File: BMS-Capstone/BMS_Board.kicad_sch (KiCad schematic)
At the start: 32 parts, among them IC1 MP2643, IC2 MP2643, Q1 FODM121, Q2 FODM121, Q3 FODM121, Q4 FODM121

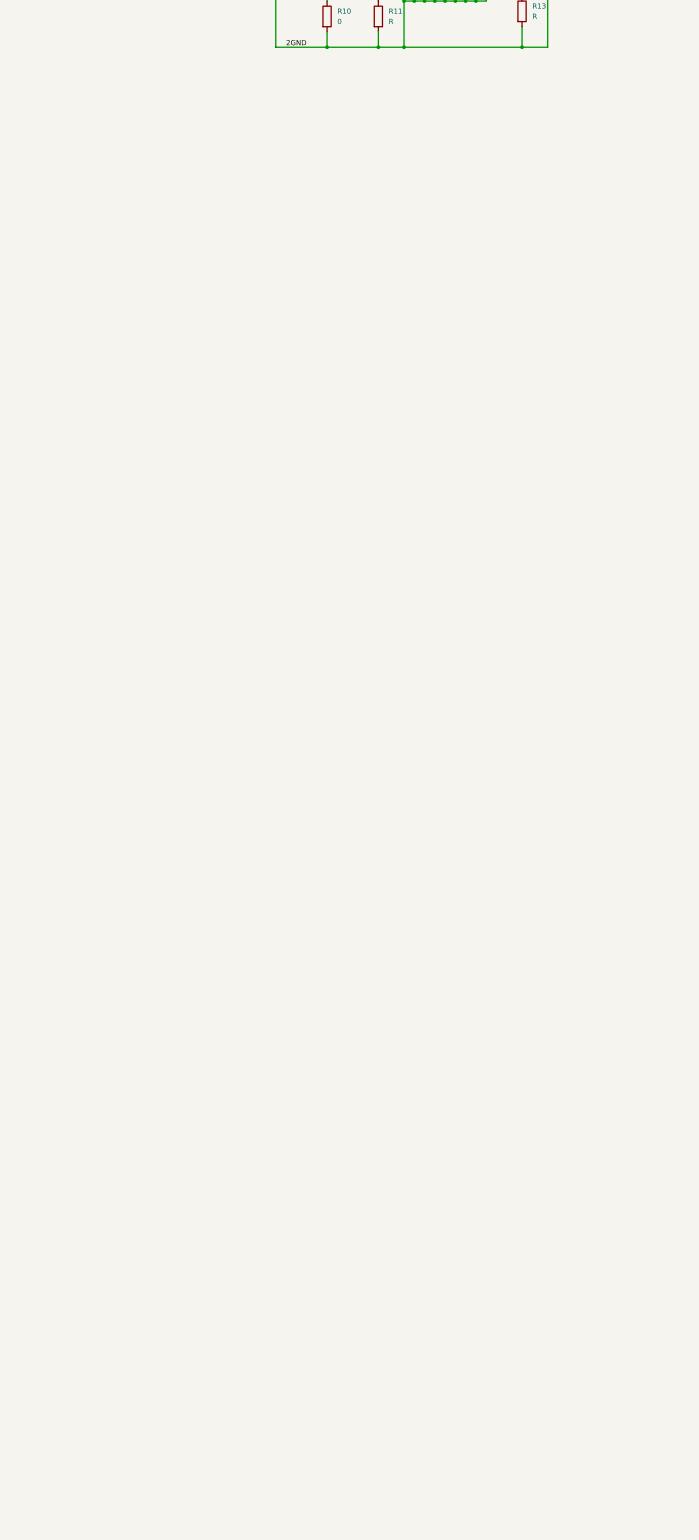
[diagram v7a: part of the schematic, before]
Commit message: Added 4 balancing boards
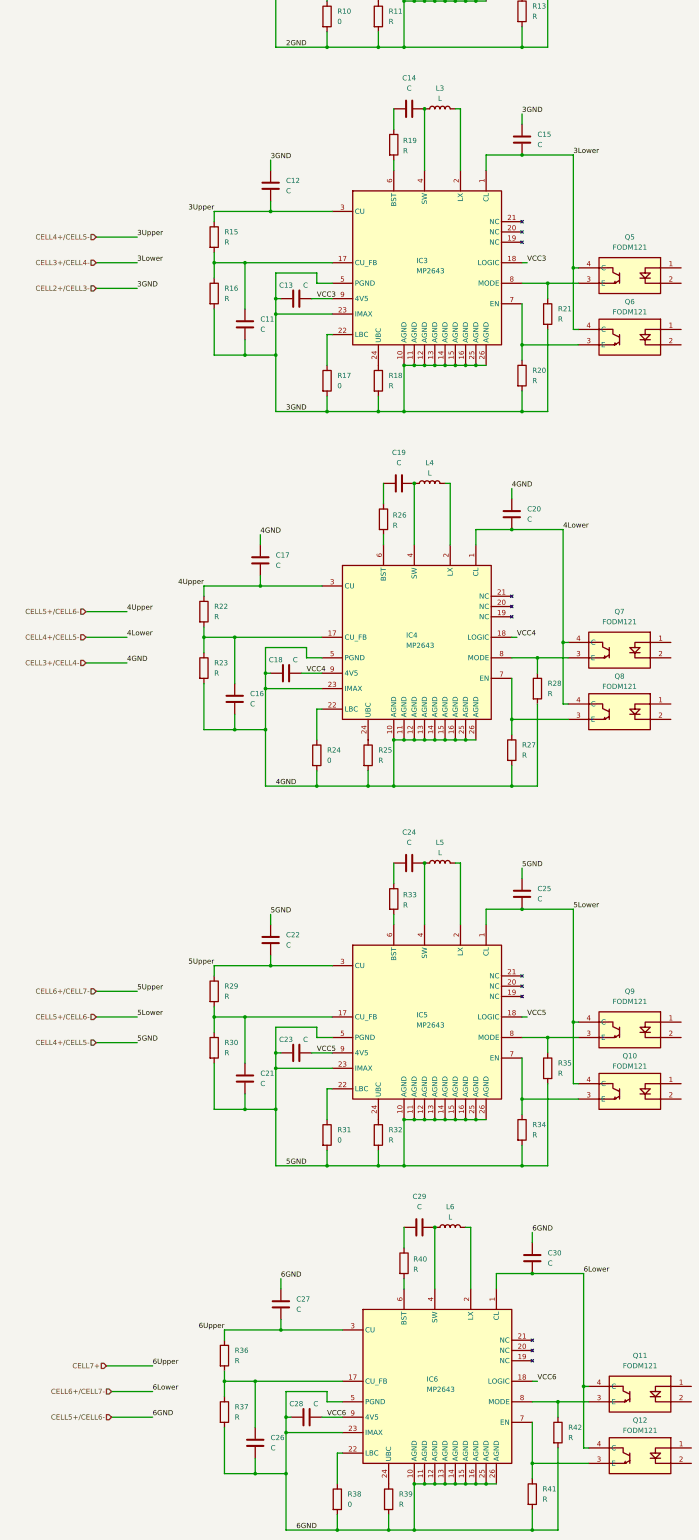
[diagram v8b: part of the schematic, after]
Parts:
- added C11, C12, C13, C14, C15, C16, C17, C18, C19, C20, C21, C22, C23, C24, C25, C26, C27, C28, C29, C30: C, Capacitor_SMD:C_0805_2012Metric, symbol Device:C
- added IC3, IC4, IC5, IC6: MP2643, SamacSys_Parts:MP2639AGRZ, symbol SamacSys_Parts:MP2643
- added L3, L4, L5, L6: L, SamacSys_Parts:MPLAL4020R47 Inductor, symbol Device:L
- added Q10, Q11, Q12, Q5, Q6, Q7, Q8, Q9: FODM121, SamacSys_Parts:SOP254P675X240-4N, symbol SamacSys_Parts:FODM121
- added R15, R16, R18, R19, R20, R21, R22, R23, R25, R26, R27, R28, R29, R30, R32, R33, R34, R35, R36, R37, R39, R40, R41, R42: R, Resistor_SMD:R_0805_2012Metric, symbol Device:R
- added R17, R24, R31, R38: 0, Resistor_SMD:R_0805_2012Metric, symbol Device:R
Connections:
- net CELL2+/CELL3-: now also C11.1, C12.2, C13.1, C15.2, IC3.10 (AGND), IC3.11 (AGND), IC3.12 (AGND), IC3.13 (AGND), IC3.14 (AGND), IC3.15 (AGND), IC3.16 (AGND), IC3.23 (IMAX), IC3.25 (AGND), IC3.26 (AGND), IC3.5 (PGND), R16.2, R17.2, R18.2, R20.2, R21.2
- net CELL3+/CELL4-: now also C15.1, C16.1, C17.2, C18.1, C20.2, IC3.1 (CL), IC4.10 (AGND), IC4.11 (AGND), IC4.12 (AGND), IC4.13 (AGND), IC4.14 (AGND), IC4.15 (AGND), IC4.16 (AGND), IC4.23 (IMAX), IC4.25 (AGND), IC4.26 (AGND), IC4.5 (PGND), Q5.4 (C), Q6.4 (C), R23.2, R24.2, R25.2, R27.2, R28.2
- new net: IC3.24 (UBC), R18.1
- new net: IC6.8 (MODE), Q11.3 (E), R42.1
- new net: IC4.22 (LBC), R24.1
- new net: C21.2, IC5.17 (CU_FB), R29.2, R30.1
- new net: C16.2, IC4.17 (CU_FB), R22.2, R23.1
- new net: C29.1, R40.1
- new net: C29.2, IC6.4 (SW), L6.1
- new net: IC3.22 (LBC), R17.1
- new net: IC4.2 (LX), L4.2
- new net: IC4.24 (UBC), R25.1
- new net: C19.2, IC4.4 (SW), L4.1
- new net: IC4.6 (BST), R26.2
- new net: IC4.7 (EN), Q8.3 (E), R27.1
- new net: IC4.8 (MODE), Q7.3 (E), R28.1
- new net: IC5.7 (EN), Q10.3 (E), R34.1
- new net: IC3.8 (MODE), Q5.3 (E), R21.1
- new net: C26.2, IC6.17 (CU_FB), R36.2, R37.1
- new net: C11.2, IC3.17 (CU_FB), R15.2, R16.1
- new net: C24.2, IC5.4 (SW), L5.1
- new net: IC5.2 (LX), L5.2
- new net: IC3.2 (LX), L3.2
- new net: C14.2, IC3.4 (SW), L3.1
- new net: IC3.6 (BST), R19.2
- new net: IC3.7 (EN), Q6.3 (E), R20.1
- new net: IC6.22 (LBC), R38.1
- new net: IC6.2 (LX), L6.2
- new net: C19.1, R26.1
- new net: IC6.24 (UBC), R39.1
- new net: IC5.22 (LBC), R31.1
- new net: IC6.7 (EN), Q12.3 (E), R41.1
- new net: C14.1, R19.1
- new net: IC5.8 (MODE), Q9.3 (E), R35.1
- new net: C24.1, R33.1
- new net: IC5.6 (BST), R33.2
- new net: IC6.6 (BST), R40.2
- new net: IC5.24 (UBC), R32.1
- new net CELL4+/CELL5-: C12.1, C20.1, C21.1, C22.2, C23.1, C25.2, IC3.3 (CU), IC4.1 (CL), IC5.10 (AGND), IC5.11 (AGND), IC5.12 (AGND), IC5.13 (AGND), IC5.14 (AGND), IC5.15 (AGND), IC5.16 (AGND), IC5.23 (IMAX), IC5.25 (AGND), IC5.26 (AGND), IC5.5 (PGND), Q7.4 (C), Q8.4 (C), R15.1, R30.2, R31.2, R32.2, R34.2, R35.2
- new net CELL5+/CELL6-: C17.1, C25.1, C26.1, C27.2, C28.1, C30.2, IC4.3 (CU), IC5.1 (CL), IC6.10 (AGND), IC6.11 (AGND), IC6.12 (AGND), IC6.13 (AGND), IC6.14 (AGND), IC6.15 (AGND), IC6.16 (AGND), IC6.23 (IMAX), IC6.25 (AGND), IC6.26 (AGND), IC6.5 (PGND), Q10.4 (C), Q9.4 (C), R22.1, R37.2, R38.2, R39.2, R41.2, R42.2
- new net CELL6+/CELL7-: C22.1, C30.1, IC5.3 (CU), IC6.1 (CL), Q11.4 (C), Q12.4 (C), R29.1
- new net CELL7+: C27.1, IC6.3 (CU), R36.1
- new net VCC3: C13.2, IC3.18 (LOGIC), IC3.9 (4V5)
- new net VCC4: C18.2, IC4.18 (LOGIC), IC4.9 (4V5)
- new net VCC5: C23.2, IC5.18 (LOGIC), IC5.9 (4V5)
- new net VCC6: C28.2, IC6.18 (LOGIC), IC6.9 (4V5)
